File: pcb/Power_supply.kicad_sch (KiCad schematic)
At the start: 33 parts, among them SW1 POWER, U1 LTC3872, U2 TLV761

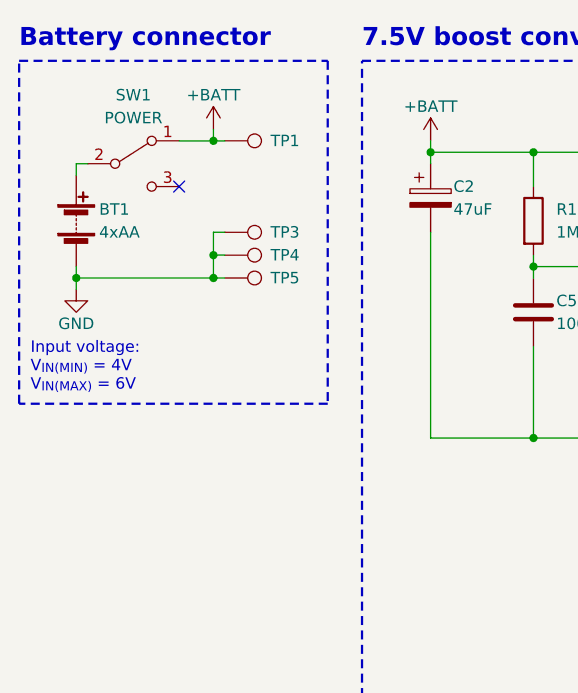
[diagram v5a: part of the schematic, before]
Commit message: [pcb] Batteries split into 2 holders
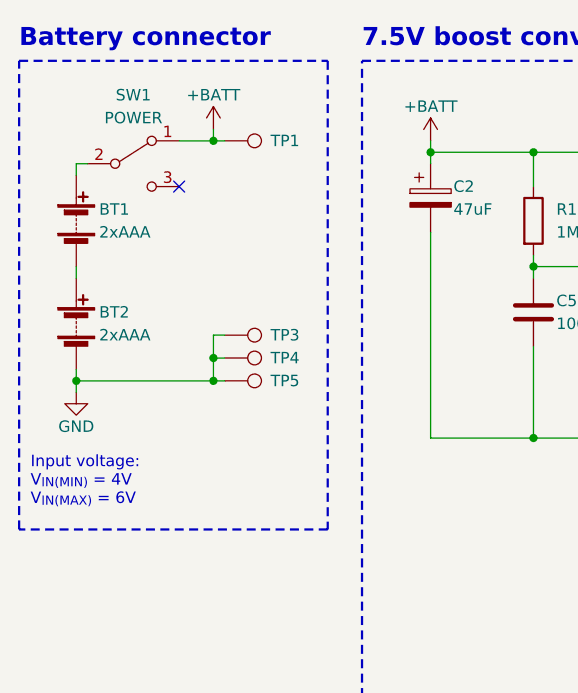
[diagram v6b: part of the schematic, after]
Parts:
- added BT2: 2xAAA, Battery:BatteryHolder_Keystone_2468_2xAAA, symbol Device:Battery
- BT1: value 4xAA -> 2xAAA; footprint Autko:Keystone_2481RB -> Battery:BatteryHolder_Keystone_2468_2xAAA
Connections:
- net GND: now also BT2.2 (-); no longer BT1.2 (-)
- new net: BT1.2 (-), BT2.1 (+)
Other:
- moved on the sheet: TP3, TP4, TP5
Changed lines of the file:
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@@
   (junction (at 39.37 27.94) (diameter 0) (color 0 0 0 0)
   )
-  (junction (at 39.37 43.18) (diameter 0) (color 0 0 0 0)
+  (junction (at 39.37 54.61) (diameter 0) (color 0 0 0 0)
   )
   (junction (at 27.94 128.27) (diameter 0) (color 0 0 0 0)
@@
   (junction (at 93.98 60.96) (diameter 0) (color 0 0 0 0)
   )
-  (junction (at 24.13 43.18) (diameter 0) (color 0 0 0 0)
+  (junction (at 24.13 54.61) (diameter 0) (color 0 0 0 0)
   )
   (junction (at 53.34 128.27) (diameter 0) (color 0 0 0 0)
@@
   (junction (at 172.72 29.21) (diameter 0) (color 0 0 0 0)
   )
-  (junction (at 39.37 40.64) (diameter 0) (color 0 0 0 0)
+  (junction (at 39.37 52.07) (diameter 0) (color 0 0 0 0)
   )
   (no_connect (at 35.56 33.02))
@@
     (stroke (width 0) (type default))
   )
+  (wire (pts (xy 24.13 41.91) (xy 24.13 43.18))
+    (stroke (width 0) (type default))
+  )
   (wire (pts (xy 40.64 138.43) (xy 53.34 138.43))
     (stroke (width 0) (type default))
@@
     (stroke (width 0) (type default))
   )
-  (wire (pts (xy 39.37 38.1) (xy 39.37 40.64))
+  (wire (pts (xy 39.37 49.53) (xy 39.37 52.07))
     (stroke (width 0) (type default))
   )
@@
     (stroke (width 0) (type default))
   )
-  (wire (pts (xy 39.37 43.18) (xy 40.64 43.18))
+  (wire (pts (xy 39.37 54.61) (xy 40.64 54.61))
     (stroke (width 0) (type default))
   )
@@
     (stroke (width 0) (type default))
   )
-  (wire (pts (xy 24.13 43.18) (xy 39.37 43.18))
+  (wire (pts (xy 24.13 54.61) (xy 39.37 54.61))
     (stroke (width 0) (type default))
   )
@@
     (stroke (width 0) (type default))
   )
-  (wire (pts (xy 39.37 40.64) (xy 39.37 43.18))
+  (wire (pts (xy 39.37 52.07) (xy 39.37 54.61))
     (stroke (width 0) (type default))
   )
@@
     (stroke (width 0) (type default))
   )
-  (wire (pts (xy 24.13 43.18) (xy 24.13 44.45))
+  (wire (pts (xy 24.13 54.61) (xy 24.13 55.88))
     (stroke (width 0) (type default))
   )
@@
     (stroke (width 0) (type default))
   )
-  (wire (pts (xy 24.13 41.91) (xy 24.13 43.18))
+  (wire (pts (xy 24.13 53.34) (xy 24.13 54.61))
     (stroke (width 0) (type default))
   )
@@
     (stroke (width 0) (type default))
   )
-  (wire (pts (xy 40.64 38.1) (xy 39.37 38.1))
+  (wire (pts (xy 40.64 49.53) (xy 39.37 49.53))
     (stroke (width 0) (type default))
   )
@@
     (stroke (width 0) (type default))
   )
-  (wire (pts (xy 40.64 40.64) (xy 39.37 40.64))
+  (wire (pts (xy 40.64 52.07) (xy 39.37 52.07))
     (stroke (width 0) (type default))
   )
@@
     (fill (type none))
   )
-  (rectangle (start 17.78 19.05) (end 52.07 57.15)
+  (rectangle (start 17.78 19.05) (end 52.07 71.12)
     (stroke (width 0.25) (type dash))
     (fill (type none))
@@
     (effects (font (size 1.27 1.27)) (justify left bottom))
   )
-  (text "Input voltage:\nV_{IN(MIN)} = 4V\nV_{IN(MAX)} = 6V" (at 19.05 55.88 0)
+  (text "Input voltage:\nV_{IN(MIN)} = 4V\nV_{IN(MAX)} = 6V" (at 19.05 68.58 0)
     (effects (font (size 1.27 1.27)) (justify left bottom))
   )
@@
     )
   )
-  (symbol (lib_id "Device:Battery") (at 24.13 36.83 0) (unit 1)
-    (in_bom yes) (on_board yes) (dnp no)
-    (property "Reference" "BT1" (at 26.67 35.56 0)
-      (effects (font (size 1.27 1.27)) (justify left))
-    )
-    (property "Value" "4xAA" (at 26.67 38.1 0)
-      (effects (font (size 1.27 1.27)) (justify left))
-    )
-    (property "Footprint" "Autko:Keystone_2481RB" (at 24.13 35.306 90)
-      (effects (font (size 1.27 1.27)) hide)
-    )
-    (property "Datasheet" "~" (at 24.13 35.306 90)
-      (effects (font (size 1.27 1.27)) hide)
-    )
-    (pin "1")
-    (pin "2")
-    (instances
-      (project "Autko"
-        (path "/8d5cfdec-de34-4148-9100-7125640c46f5/c078ece0-fea4-45db-aa95-3799eb753f2b"
-          (reference "BT1") (unit 1)
-        )
-      )
-    )
-  )
   (symbol (lib_id "Device:LED") (at 96.52 123.19 90) (unit 1)
     (in_bom yes) (on_board yes) (dnp no)
@@
     )
   )
-  (symbol (lib_id "Connector:TestPoint") (at 40.64 38.1 270) (unit 1)
-    (in_bom yes) (on_board yes) (dnp no)
-    (property "Reference" "TP3" (at 45.72 38.1 90)
-      (effects (font (size 1.27 1.27)) (justify left))
-    )
-    (property "Value" "TestPoint" (at 42.037 40.64 0)
+  (symbol (lib_id "Connector:TestPoint") (at 40.64 49.53 270) (unit 1)
+    (in_bom yes) (on_board yes) (dnp no)
+    (property "Reference" "TP3" (at 45.72 49.53 90)
+      (effects (font (size 1.27 1.27)) (justify left))
+    )
+    (property "Value" "TestPoint" (at 42.037 52.07 0)
       (effects (font (size 1.27 1.27)) (justify left) hide)
     )
-    (property "Footprint" "TestPoint:TestPoint_Keystone_5019_Minature" (at 40.64 43.18 0)
-      (effects (font (size 1.27 1.27)) hide)
-    )
-    (property "Datasheet" "~" (at 40.64 43.18 0)
+    (property "Footprint" "TestPoint:TestPoint_Keystone_5019_Minature" (at 40.64 54.61 0)
+      (effects (font (size 1.27 1.27)) hide)
+    )
+    (property "Datasheet" "~" (at 40.64 54.61 0)
       (effects (font (size 1.27 1.27)) hide)
     )
@@
     )
   )
-  (symbol (lib_id "Connector:TestPoint") (at 40.64 43.18 270) (unit 1)
-    (in_bom yes) (on_board yes) (dnp no)
-    (property "Reference" "TP5" (at 45.72 43.18 90)
-      (effects (font (size 1.27 1.27)) (justify left))
-    )
-    (property "Value" "TestPoint" (at 42.037 45.72 0)
+  (symbol (lib_id "Connector:TestPoint") (at 40.64 54.61 270) (unit 1)
+    (in_bom yes) (on_board yes) (dnp no)
+    (property "Reference" "TP5" (at 45.72 54.61 90)
+      (effects (font (size 1.27 1.27)) (justify left))
+    )
+    (property "Value" "TestPoint" (at 42.037 57.15 0)
       (effects (font (size 1.27 1.27)) (justify left) hide)
     )
-    (property "Footprint" "TestPoint:TestPoint_Keystone_5019_Minature" (at 40.64 48.26 0)
-      (effects (font (size 1.27 1.27)) hide)
-    )
-    (property "Datasheet" "~" (at 40.64 48.26 0)
+    (property "Footprint" "TestPoint:TestPoint_Keystone_5019_Minature" (at 40.64 59.69 0)
+      (effects (font (size 1.27 1.27)) hide)
+    )
+    (property "Datasheet" "~" (at 40.64 59.69 0)
       (effects (font (size 1.27 1.27)) hide)
     )
@@
         (path "/8d5cfdec-de34-4148-9100-7125640c46f5/c078ece0-fea4-45db-aa95-3799eb753f2b"
           (reference "C8") (unit 1)
+        )
+      )
+    )
+  )
+  (symbol (lib_id "Device:Battery") (at 24.13 48.26 0) (unit 1)
+    (in_bom yes) (on_board yes) (dnp no)
+    (property "Reference" "BT2" (at 26.67 46.99 0)
+      (effects (font (size 1.27 1.27)) (justify left))
+    )
+    (property "Value" "2xAAA" (at 26.67 49.53 0)
+      (effects (font (size 1.27 1.27)) (justify left))
+    )
+    (property "Footprint" "Battery:BatteryHolder_Keystone_2468_2xAAA" (at 24.13 46.736 90)
+      (effects (font (size 1.27 1.27)) hide)
+    )
+    (property "Datasheet" "~" (at 24.13 46.736 90)
+      (effects (font (size 1.27 1.27)) hide)
+    )
+    (pin "1")
+    (pin "2")
+    (instances
+      (project "Autko"
+        (path "/8d5cfdec-de34-4148-9100-7125640c46f5/c078ece0-fea4-45db-aa95-3799eb753f2b"
+          (reference "BT2") (unit 1)
         )
       )
@@
     )
   )
-  (symbol (lib_id "power:GND") (at 24.13 44.45 0) (unit 1)
-    (in_bom yes) (on_board yes) (dnp no)
-    (property "Reference" "#PWR05" (at 24.13 50.8 0)
-      (effects (font (size 1.27 1.27)) hide)
-    )
-    (property "Value" "GND" (at 24.13 48.26 0)
-      (effects (font (size 1.27 1.27)))
-    )
-    (property "Footprint" "" (at 24.13 44.45 0)
-      (effects (font (size 1.27 1.27)) hide)
-    )
-    (property "Datasheet" "" (at 24.13 44.45 0)
+  (symbol (lib_id "power:GND") (at 24.13 55.88 0) (unit 1)
+    (in_bom yes) (on_board yes) (dnp no)
+    (property "Reference" "#PWR05" (at 24.13 62.23 0)
+      (effects (font (size 1.27 1.27)) hide)
+    )
+    (property "Value" "GND" (at 24.13 59.69 0)
+      (effects (font (size 1.27 1.27)))
+    )
+    (property "Footprint" "" (at 24.13 55.88 0)
+      (effects (font (size 1.27 1.27)) hide)
+    )
+    (property "Datasheet" "" (at 24.13 55.88 0)
       (effects (font (size 1.27 1.27)) hide)
     )
@@
     )
   )
-  (symbol (lib_id "Connector:TestPoint") (at 40.64 40.64 270) (unit 1)
-    (in_bom yes) (on_board yes) (dnp no)
-    (property "Reference" "TP4" (at 45.72 40.64 90)
-      (effects (font (size 1.27 1.27)) (justify left))
-    )
-    (property "Value" "TestPoint" (at 42.037 43.18 0)
+  (symbol (lib_id "Device:Battery") (at 24.13 36.83 0) (unit 1)
+    (in_bom yes) (on_board yes) (dnp no)
+    (property "Reference" "BT1" (at 26.67 35.56 0)
+      (effects (font (size 1.27 1.27)) (justify left))
+    )
+    (property "Value" "2xAAA" (at 26.67 38.1 0)
+      (effects (font (size 1.27 1.27)) (justify left))
+    )
+    (property "Footprint" "Battery:BatteryHolder_Keystone_2468_2xAAA" (at 24.13 35.306 90)
+      (effects (font (size 1.27 1.27)) hide)
+    )
+    (property "Datasheet" "~" (at 24.13 35.306 90)
+      (effects (font (size 1.27 1.27)) hide)
+    )
+    (pin "1")
+    (pin "2")
+    (instances
+      (project "Autko"
+        (path "/8d5cfdec-de34-4148-9100-7125640c46f5/c078ece0-fea4-45db-aa95-3799eb753f2b"
+          (reference "BT1") (unit 1)
+        )
+      )
+    )
+  )
+  (symbol (lib_id "Connector:TestPoint") (at 40.64 52.07 270) (unit 1)
+    (in_bom yes) (on_board yes) (dnp no)
+    (property "Reference" "TP4" (at 45.72 52.07 90)
+      (effects (font (size 1.27 1.27)) (justify left))
+    )
+    (property "Value" "TestPoint" (at 42.037 54.61 0)
       (effects (font (size 1.27 1.27)) (justify left) hide)
     )
-    (property "Footprint" "TestPoint:TestPoint_Keystone_5019_Minature" (at 40.64 45.72 0)
-      (effects (font (size 1.27 1.27)) hide)
-    )
-    (property "Datasheet" "~" (at 40.64 45.72 0)
-      (effects (font (size 1.27 1.27)) hide)
-    )
+    (property "Footprint" "TestPoint:TestPoint_Keystone_5019_Minature" (at 40.64 57.15 0)
+      (effects (font (size 1.27 1.27)) hide)
+    )
+    (property "Datasheet" "~" (at 40.64 57.15 0)
+      (effects (font (size 1.27 1.27)) hide)
+    )

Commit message: [pcb] Routing on smaller board. Before removal of button.
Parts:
- L1: footprint Inductor_SMD:L_12x12mm_H6mm -> Autko:Coilcraft_MSS1260
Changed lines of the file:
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@@
       (effects (font (size 1.27 1.27)))
     )
-    (property "Footprint" "Inductor_SMD:L_12x12mm_H6mm" (at 125.73 29.21 0)
+    (property "Footprint" "Autko:Coilcraft_MSS1260" (at 125.73 29.21 0)
       (effects (font (size 1.27 1.27)) hide)
     )
